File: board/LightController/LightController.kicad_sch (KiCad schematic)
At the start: 11 parts, among them J1 Jack-DC, J2 Light bank 1, J3 Light Bank 2, J4 Light Bank 3, U1 CPC1002N, U2 AP63205WU, U3 FeatherS2

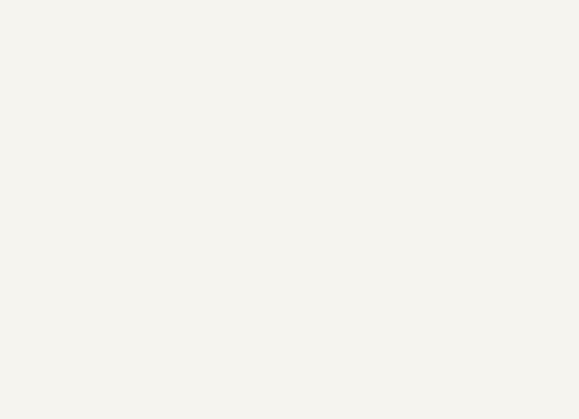
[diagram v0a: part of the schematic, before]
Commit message: Add mounting holes.
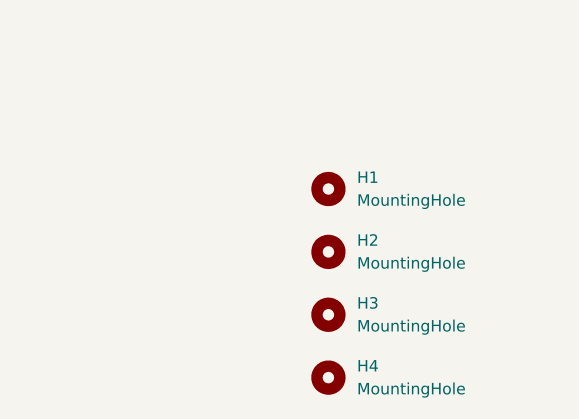
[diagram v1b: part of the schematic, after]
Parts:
- added H1, H2, H3, H4: MountingHole, MountingHole:MountingHole_2mm, symbol Mechanical:MountingHole
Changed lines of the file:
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@@
     (pin "2")
+  )
+  (symbol (lib_id "Mechanical:MountingHole") (at 258.445 129.54 0) (unit 1)
+    (in_bom yes) (on_board yes) (fields_autoplaced)
+    (property "Reference" "H1" (id 0) (at 261.62 128.2699 0)
+      (effects (font (size 1.27 1.27)) (justify left))
+    )
+    (property "Value" "MountingHole" (id 1) (at 261.62 130.8099 0)
+      (effects (font (size 1.27 1.27)) (justify left))
+    )
+    (property "Footprint" "MountingHole:MountingHole_2mm" (id 2) (at 258.445 129.54 0)
+      (effects (font (size 1.27 1.27)) hide)
+    )
+    (property "Datasheet" "~" (id 3) (at 258.445 129.54 0)
+      (effects (font (size 1.27 1.27)) hide)
+    )
   )
   (symbol (lib_id "cmumford:FeatherS2") (at 189.23 88.9 0) (unit 1)
@@
     (pin "1")
   )
+  (symbol (lib_id "Mechanical:MountingHole") (at 258.445 150.495 0) (unit 1)
+    (in_bom yes) (on_board yes) (fields_autoplaced)
+    (property "Reference" "H4" (id 0) (at 261.62 149.2249 0)
+      (effects (font (size 1.27 1.27)) (justify left))
+    )
+    (property "Value" "MountingHole" (id 1) (at 261.62 151.7649 0)
+      (effects (font (size 1.27 1.27)) (justify left))
+    )
+    (property "Footprint" "MountingHole:MountingHole_2mm" (id 2) (at 258.445 150.495 0)
+      (effects (font (size 1.27 1.27)) hide)
+    )
+    (property "Datasheet" "~" (id 3) (at 258.445 150.495 0)
+      (effects (font (size 1.27 1.27)) hide)
+    )
+  )
   (symbol (lib_id "Connector:Conn_01x05_Female") (at 264.16 35.56 0) (unit 1)
     (in_bom yes) (on_board yes) (fields_autoplaced)
@@
     (pin "1")
     (pin "2")
+  )
+  (symbol (lib_id "Mechanical:MountingHole") (at 258.445 136.525 0) (unit 1)
+    (in_bom yes) (on_board yes) (fields_autoplaced)
+    (property "Reference" "H2" (id 0) (at 261.62 135.2549 0)
+      (effects (font (size 1.27 1.27)) (justify left))
+    )
+    (property "Value" "MountingHole" (id 1) (at 261.62 137.7949 0)
+      (effects (font (size 1.27 1.27)) (justify left))
+    )
+    (property "Footprint" "MountingHole:MountingHole_2mm" (id 2) (at 258.445 136.525 0)
+      (effects (font (size 1.27 1.27)) hide)
+    )
+    (property "Datasheet" "~" (id 3) (at 258.445 136.525 0)
+      (effects (font (size 1.27 1.27)) hide)
+    )
   )
   (symbol (lib_id "Device:C") (at 48.26 52.07 0) (unit 1)
@@
     (pin "4")
   )
+  (symbol (lib_id "Mechanical:MountingHole") (at 258.445 143.51 0) (unit 1)
+    (in_bom yes) (on_board yes) (fields_autoplaced)
+    (property "Reference" "H3" (id 0) (at 261.62 142.2399 0)
+      (effects (font (size 1.27 1.27)) (justify left))
+    )
+    (property "Value" "MountingHole" (id 1) (at 261.62 144.7799 0)
+      (effects (font (size 1.27 1.27)) (justify left))
+    )
+    (property "Footprint" "MountingHole:MountingHole_2mm" (id 2) (at 258.445 143.51 0)
+      (effects (font (size 1.27 1.27)) hide)
+    )
+    (property "Datasheet" "~" (id 3) (at 258.445 143.51 0)
+      (effects (font (size 1.27 1.27)) hide)
+    )
+  )
   (symbol (lib_id "power:GND") (at 257.81 76.2 0) (unit 1)
     (in_bom yes) (on_board yes) (fields_autoplaced)
@@
       (reference "C3") (unit 1) (value "2x22µF") (footprint "Capacitor_SMD:C_0805_2012Metric")
     )
+    (path "/5fdabda6-9c9c-427b-87e5-a291030a9854"
+      (reference "H1") (unit 1) (value "MountingHole") (footprint "MountingHole:MountingHole_2mm")
+    )
+    (path "/cfd70de8-7eae-4963-bce1-9ab8e2e2645a"
+      (reference "H2") (unit 1) (value "MountingHole") (footprint "MountingHole:MountingHole_2mm")
+    )
+    (path "/f6457ab7-4a5a-4cfc-a380-dadf7e28b0f0"
+      (reference "H3") (unit 1) (value "MountingHole") (footprint "MountingHole:MountingHole_2mm")
+    )
+    (path "/88443d63-141a-46a6-9595-3fe62dde3e1c"
+      (reference "H4") (unit 1) (value "MountingHole") (footprint "MountingHole:MountingHole_2mm")
+    )
     (path "/266d8892-601b-4e63-a039-25514b95a912"

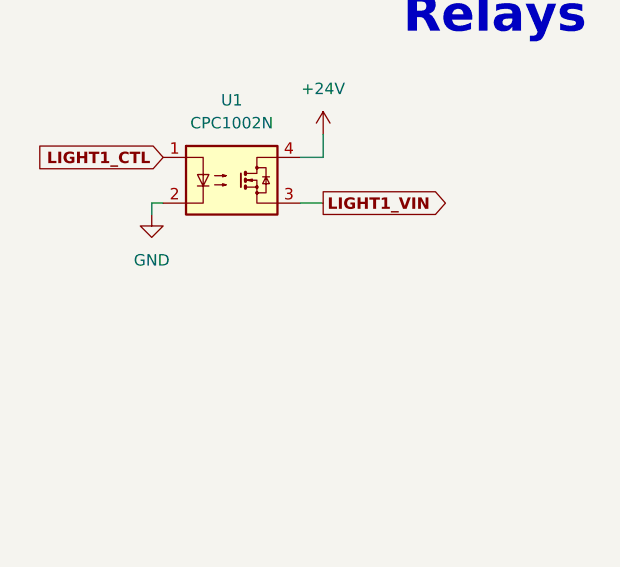
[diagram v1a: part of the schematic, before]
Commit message: Increase trace width and relay input resistor.
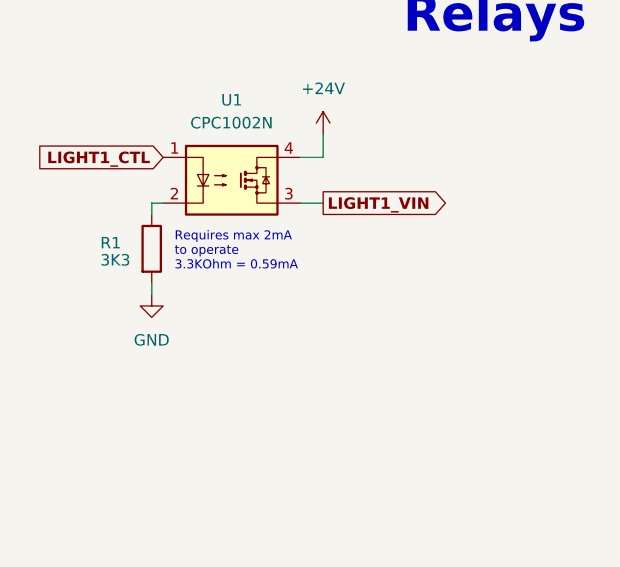
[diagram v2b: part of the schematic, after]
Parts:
- added R1: 3K3, Resistor_SMD:R_0805_2012Metric, symbol Device:R
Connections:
- net GND: now also R1.2; no longer U1.2
- new net: R1.1, U1.2
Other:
- note added: "Requires max 2mA to operate 3.3KOhm = 0.59mA"
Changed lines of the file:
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@@
+    (stroke (width 0) (type default) (color 0 0 0 0))
+  )
+  (wire (pts (xy 31.75 111.76) (xy 31.75 113.03))
     (stroke (width 0) (type default) (color 0 0 0 0))
   )
@@
   (text "MCU" (at 182.88 57.15 0)
     (effects (font (size 4 4) (thickness 0.8) bold) (justify left bottom))
+  )
+  (text "Requires max 2mA\nto operate\n3.3KOhm = 0.59mA" (at 34.29 110.49 0)
+    (effects (font (size 1 1)) (justify left bottom))
   )
   (text "Connectors" (at 243.84 22.86 0)
@@
     (pin "1")
   )
-  (symbol (lib_id "power:GND") (at 31.75 104.14 0) (unit 1)
-    (in_bom yes) (on_board yes) (fields_autoplaced)
-    (property "Reference" "#PWR01" (id 0) (at 31.75 110.49 0)
-      (effects (font (size 1.27 1.27)) hide)
-    )
-    (property "Value" "GND" (id 1) (at 31.75 109.22 0))
-    (property "Footprint" "" (id 2) (at 31.75 104.14 0)
-      (effects (font (size 1.27 1.27)) hide)
-    )
-    (property "Datasheet" "" (id 3) (at 31.75 104.14 0)
+  (symbol (lib_id "power:GND") (at 31.75 113.03 0) (unit 1)
+    (in_bom yes) (on_board yes) (fields_autoplaced)
+    (property "Reference" "#PWR01" (id 0) (at 31.75 119.38 0)
+      (effects (font (size 1.27 1.27)) hide)
+    )
+    (property "Value" "GND" (id 1) (at 31.75 118.11 0))
+    (property "Footprint" "" (id 2) (at 31.75 113.03 0)
+      (effects (font (size 1.27 1.27)) hide)
+    )
+    (property "Datasheet" "" (id 3) (at 31.75 113.03 0)
       (effects (font (size 1.27 1.27)) hide)
     )
@@
     )
     (property "Datasheet" "~" (id 3) (at 48.26 52.07 0)
+      (effects (font (size 1.27 1.27)) hide)
+    )
+    (pin "1")
+    (pin "2")
+  )
+  (symbol (lib_id "Device:R") (at 31.75 107.95 0) (unit 1)
+    (in_bom yes) (on_board yes)
+    (property "Reference" "R1" (id 0) (at 26.035 107.315 0)
+      (effects (font (size 1.27 1.27)) (justify left))
+    )
+    (property "Value" "3K3" (id 1) (at 26.035 109.22 0)
+      (effects (font (size 1.27 1.27)) (justify left))
+    )
+    (property "Footprint" "Resistor_SMD:R_0805_2012Metric" (id 2) (at 29.972 107.95 90)
+      (effects (font (size 1.27 1.27)) hide)
+    )
+    (property "Datasheet" "~" (id 3) (at 31.75 107.95 0)
       (effects (font (size 1.27 1.27)) hide)
     )
@@
       (reference "L1") (unit 1) (value "4.7µH") (footprint "Inductor_SMD:L_0805_2012Metric")
     )
+    (path "/d9cc0ec6-44ef-4560-bf00-1b2db1182362"
+      (reference "R1") (unit 1) (value "3K3") (footprint "Resistor_SMD:R_0805_2012Metric")
+    )
     (path "/f0df37d1-af5b-4560-a103-ec9ded8246fe"

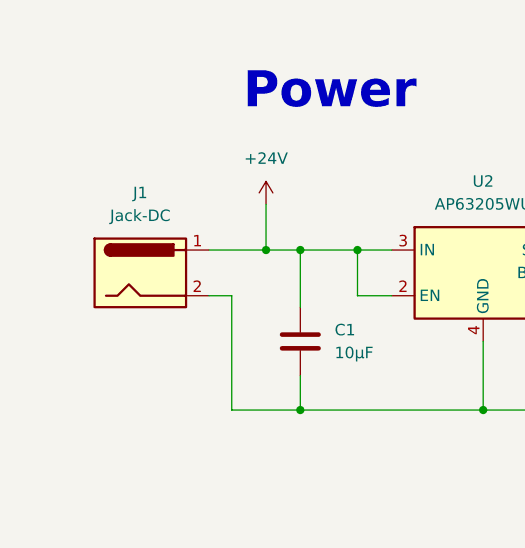
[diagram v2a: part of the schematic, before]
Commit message: Using PJ-051AH barrel DC power jack.
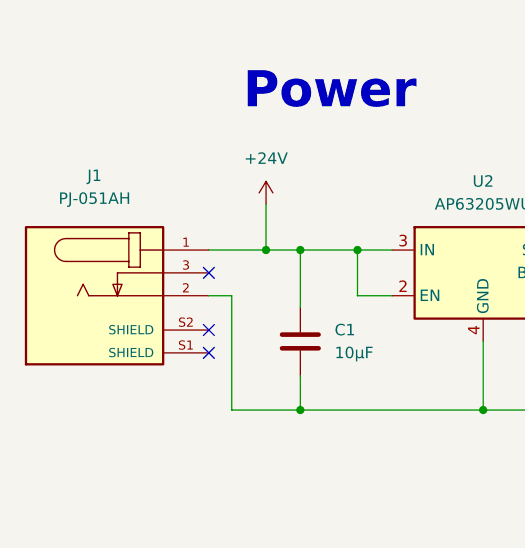
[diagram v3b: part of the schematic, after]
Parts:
- removed J1: Jack-DC, Connector_BarrelJack:BarrelJack_SwitchcraftConxall_RAPC10U_Horizontal, symbol Connector:Jack-DC
- added J1: PJ-051AH, cmumford:PJ-051AH, symbol cmumford:PJ-051AH
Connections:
- net +24V: now also J1.1
- net GND: now also J1.2
- no-connect marks 36 -> 39
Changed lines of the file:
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@@
   (junction (at 76.2 59.69) (diameter 0) (color 0 0 0 0)
   )
+  (no_connect (at 38.1 53.34))
   (no_connect (at 199.39 93.98))
   (no_connect (at 199.39 96.52))
@@
   (no_connect (at 177.8 104.14))
   (no_connect (at 177.8 99.06))
+  (no_connect (at 38.1 44.45))
+  (no_connect (at 38.1 50.8))
   (no_connect (at 259.08 50.8))
   (no_connect (at 259.08 53.34))
@@
     )
     (pin "1")
-  )
-  (symbol (lib_id "Connector:Jack-DC") (at 30.48 44.45 0) (unit 1)
-    (in_bom yes) (on_board yes) (fields_autoplaced)
-    (property "Reference" "J1" (id 0) (at 30.48 35.56 0))
-    (property "Value" "Jack-DC" (id 1) (at 30.48 38.1 0))
-    (property "Footprint" "Connector_BarrelJack:BarrelJack_SwitchcraftConxall_RAPC10U_Horizontal" (id 2) (at 31.75 45.466 0)
-      (effects (font (size 1.27 1.27)) hide)
-    )
-    (property "Datasheet" "~" (id 3) (at 31.75 45.466 0)
-      (effects (font (size 1.27 1.27)) hide)
-    )
-    (pin "1")
-    (pin "2")
   )
   (symbol (lib_id "power:+24V") (at 44.45 36.83 0) (unit 1)
@@
     (pin "9")
   )
+  (symbol (lib_id "cmumford:PJ-051AH") (at 25.4 46.99 0) (unit 1)
+    (in_bom yes) (on_board yes) (fields_autoplaced)
+    (property "Reference" "J1" (id 0) (at 25.4 33.655 0))
+    (property "Value" "PJ-051AH" (id 1) (at 25.4 36.195 0))
+    (property "Footprint" "cmumford:PJ-051AH" (id 2) (at 26.67 60.96 0)
+      (effects (font (size 1.27 1.27)) (justify left bottom) hide)
+    )
+    (property "Datasheet" "https://www.cuidevices.com/product/resource/pj-051ah.pdf" (id 3) (at 6.35 36.83 0)
+      (effects (font (size 1.27 1.27)) (justify left bottom) hide)
+    )
+    (property "PARTREV" "1.03" (id 4) (at 12.7 48.26 0)
+      (effects (font (size 1.27 1.27)) (justify left bottom) hide)
+    )
+    (property "STANDARD" "Manufacturer Recommendations" (id 5) (at 15.24 58.42 0)
+      (effects (font (size 1.27 1.27)) (justify left bottom) hide)
+    )
+    (property "MANUFACTURER" "CUI Inc." (id 6) (at 15.24 60.96 0)
+      (effects (font (size 1.27 1.27)) (justify left bottom) hide)
+    )
+    (pin "1")
+    (pin "2")
+    (pin "3")
+    (pin "S1")
+    (pin "S2")
+  )
   (symbol (lib_id "power:GND") (at 257.81 59.69 0) (unit 1)
     (in_bom yes) (on_board yes) (fields_autoplaced)
@@
       (reference "H4") (unit 1) (value "MountingHole") (footprint "MountingHole:MountingHole_2mm")
     )
-    (path "/266d8892-601b-4e63-a039-25514b95a912"
-      (reference "J1") (unit 1) (value "Jack-DC") (footprint "Connector_BarrelJack:BarrelJack_SwitchcraftConxall_RAPC10U_Horizontal")
+    (path "/66afa8a6-3bbf-4e64-9611-2fc71743ad80"
+      (reference "J1") (unit 1) (value "PJ-051AH") (footprint "cmumford:PJ-051AH")
     )
     (path "/aece2389-d92e-40a1-adae-cebd37c40ae1"

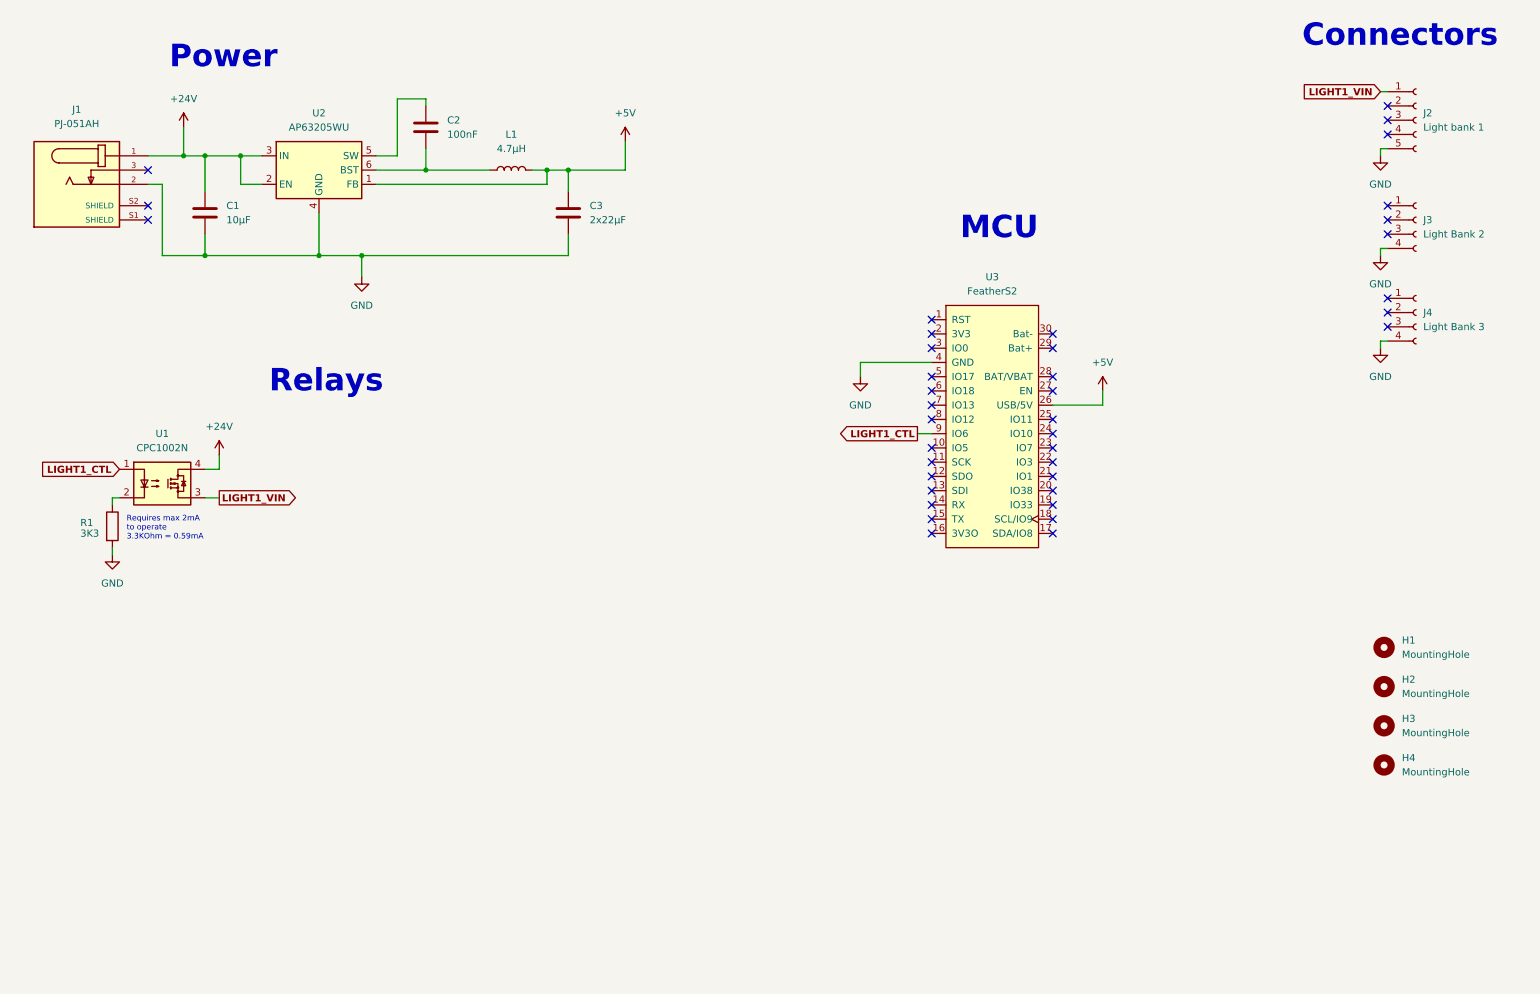
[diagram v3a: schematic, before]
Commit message: All 10 relays.
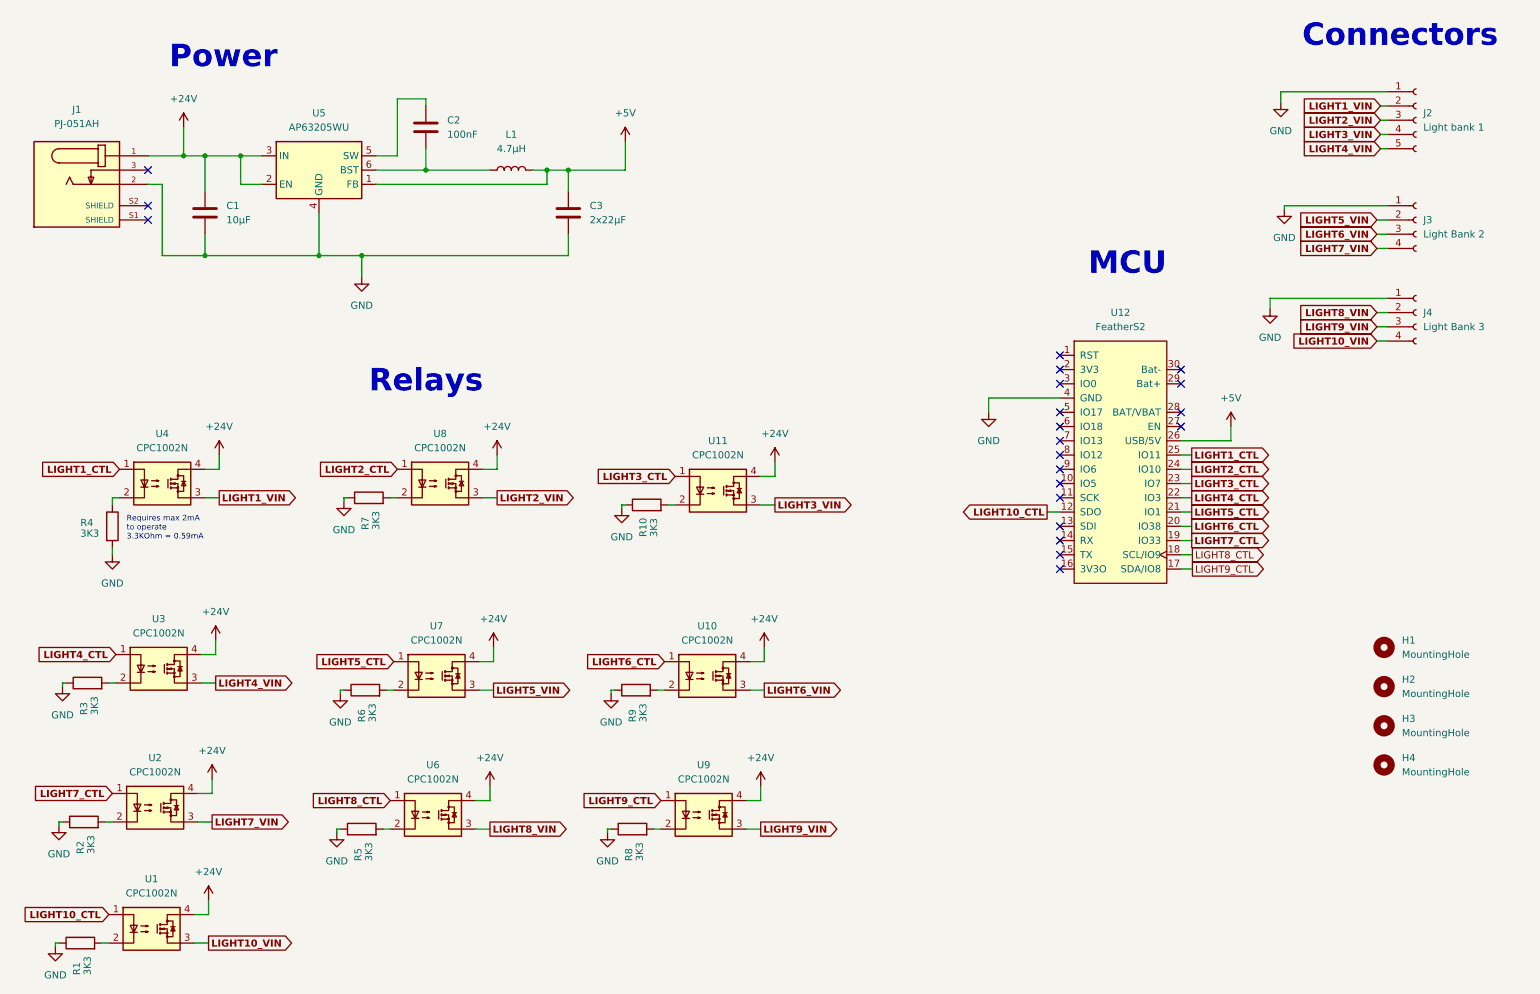
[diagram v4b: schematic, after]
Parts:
- added R1, R10, R2, R3, R5, R6, R7, R8, R9: 3K3, Resistor_SMD:R_0805_2012Metric, symbol Device:R
- added U1, U10, U11, U2, U3, U6, U7, U8, U9: CPC1002N, Package_SO:SOP-4_3.8x4.1mm_P2.54mm, symbol Relay_SolidState:CPC1002N
- renumbered R1 to R4, U3 to U12, U1 to U4, U2 to U5
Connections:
- net +24V: now also U1.4, U10.4, U11.4, U2.4, U3.4, U6.4, U7.4, U8.4, U9.4
- net GND: now also J2.1 (Pin_1), J3.1 (Pin_1), J4.1 (Pin_1), R1.1, R10.1, R2.1, R3.1, R5.1, R6.1, R7.1, R8.1, R9.1; no longer J2.5 (Pin_5), J3.4 (Pin_4), J4.4 (Pin_4)
- net LIGHT1_CTL: now also U12.25 (IO11); no longer U12.9 (IO6)
- net LIGHT1_VIN: now also J2.2 (Pin_2); no longer J2.1 (Pin_1)
- net LIGHT8_VIN: now reaches J4.2 (Pin_2)
- net LIGHT8_VIN: now also U6.3
- net LIGHT9_VIN: now reaches J4.3 (Pin_3)
- net LIGHT9_VIN: now also U9.3
- net LIGHT10_CTL: now reaches U12.12 (SDO)
- net LIGHT10_CTL: now also U1.1
- net LIGHT9_CTL: now reaches U12.17 (SDA/IO8)
- net LIGHT9_CTL: now also U9.1
- net LIGHT8_CTL: now reaches U12.18 (SCL/IO9)
- net LIGHT8_CTL: now also U6.1
- net LIGHT7_CTL: now reaches U12.19 (IO33)
- net LIGHT7_CTL: now also U2.1
- net LIGHT6_CTL: now reaches U12.20 (IO38)
- net LIGHT6_CTL: now also U10.1
- net LIGHT5_CTL: now reaches U12.21 (IO1)
- net LIGHT5_CTL: now also U7.1
- net LIGHT4_CTL: now reaches U12.22 (IO3)
- net LIGHT4_CTL: now also U3.1
- net LIGHT3_CTL: now reaches U12.23 (IO7)
- net LIGHT3_CTL: now also U11.1
- net LIGHT2_CTL: now reaches U12.24 (IO10)
- net LIGHT2_CTL: now also U8.1
- net LIGHT2_VIN: now reaches J2.3 (Pin_3)
- net LIGHT2_VIN: now also U8.3
- net LIGHT3_VIN: now reaches J2.4 (Pin_4)
- net LIGHT3_VIN: now also U11.3
- net LIGHT5_VIN: now reaches J3.2 (Pin_2)
- net LIGHT5_VIN: now also U7.3
- net LIGHT6_VIN: now reaches J3.3 (Pin_3)
- net LIGHT6_VIN: now also U10.3
- new net: R5.2, U6.2
- new net: R6.2, U7.2
- new net: R8.2, U9.2
- new net: R7.2, U8.2
- new net: R10.2, U11.2
- new net: R9.2, U10.2
- new net: R3.2, U3.2
- new net: R1.2, U1.2
- new net: R2.2, U2.2
- new net LIGHT10_VIN: J4.4 (Pin_4), U1.3
- new net LIGHT4_VIN: J2.5 (Pin_5), U3.3
- new net LIGHT7_VIN: J3.4 (Pin_4), U2.3
- no-connect marks 39 -> 21
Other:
- moved on the sheet: U12
